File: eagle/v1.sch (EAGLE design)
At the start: 40 parts, among them IC2 LT1761, IC4 LT1376-ADJ, Q1 12Mhz, T1 Si2301DS, X1 USB-MICROB

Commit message: small change
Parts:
- R6: value 15k -> 680k
- R7: value 15k -> 220k
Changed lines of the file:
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@@
 <part name="SCK" library="wirepad" deviceset="SMD5" device=""/>
 <part name="L2" library="seb" deviceset="PIS2408" device="" value="20µH/xxx mA"/>
-<part name="R6" library="rcl" deviceset="R-EU_" device="R0402" value="15k"/>
-<part name="R7" library="rcl" deviceset="R-EU_" device="R0402" value="15k"/>
+<part name="R6" library="rcl" deviceset="R-EU_" device="R0402" value="680k"/>
+<part name="R7" library="rcl" deviceset="R-EU_" device="R0402" value="220k"/>
 <part name="GND6" library="supply1" deviceset="GND" device=""/>
 <part name="P+5" library="supply1" deviceset="+12V" device=""/>

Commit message: i2c connector
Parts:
- added 3V3, GN, SCL, SDA: (no value), wirepad:SMD2
- added C13: 1µF, SparkFun-Capacitors:CAP0805
- added R12, R13: 15k, rcl:R-EU_R0402
- added U$1: MAKE-DD_LOGO'PROMPT', seb:MAKE-DD_LOGO'PROMPT'
- renumbered BL/SW2 to BL
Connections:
- new net SCL: IC1.PIO0_4/SCL-(20MA_SINK), R13.2, SCL.P
- new net SDA: IC1.PIO0_5/SDA-(20MA_SINK), R12.2, SDA.P
- net +3V3: now also 3V3.P, R12.1, R13.1
- net ADC: now also C13.1
- net GND: now also C13.2, GN.P
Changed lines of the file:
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@@
 <part name="R5" library="rcl" deviceset="R-EU_" device="R0402" value="33R"/>
 <part name="RST" library="seb" deviceset="SWITCH_MCTAEF" device=""/>
-<part name="BL/SW2" library="seb" deviceset="SWITCH_MCTAEF" device=""/>
+<part name="BL" library="seb" deviceset="SWITCH_MCTAEF" device=""/>
 <part name="C3" library="rcl" deviceset="C-EU" device="C0402" value="22pF"/>
 <part name="C2" library="rcl" deviceset="C-EU" device="C0402" value="22pF"/>
@@
 <part name="GND7" library="supply1" deviceset="GND" device=""/>
 <part name="D1" library="seb" deviceset="DIODE_0805" device="" value="4148"/>
+<part name="C13" library="SparkFun-Capacitors" deviceset="CAP" device="0805" value="1µF"/>
+<part name="GND9" library="supply1" deviceset="GND" device=""/>
+<part name="U$1" library="seb" deviceset="MAKE-DD_LOGO" device="'PROMPT'"/>
+<part name="GN" library="wirepad" deviceset="SMD2" device=""/>
+<part name="3V3" library="wirepad" deviceset="SMD2" device=""/>
+<part name="SCL" library="wirepad" deviceset="SMD2" device=""/>
+<part name="SDA" library="wirepad" deviceset="SMD2" device=""/>
+<part name="GND13" library="supply1" deviceset="GND" device=""/>
+<part name="+3V6" library="supply1" deviceset="+3V3" device=""/>
+<part name="R12" library="rcl" deviceset="R-EU_" device="R0402" value="15k"/>
+<part name="R13" library="rcl" deviceset="R-EU_" device="R0402" value="15k"/>
 </parts>
 <sheets>
@@
 <attribute name="NAME" x="259.715" y="21.59" size="1.778" layer="95"/>
 </instance>
-<instance part="BL/SW2" gate="G$1" x="274.32" y="25.4" smashed="yes"/>
+<instance part="BL" gate="G$1" x="274.32" y="25.4" smashed="yes"/>
 <instance part="C3" gate="G$1" x="27.94" y="83.82" rot="R90"/>
 <instance part="C2" gate="G$1" x="27.94" y="88.9" rot="R90"/>
@@
 <instance part="P+6" gate="1" x="83.82" y="132.08"/>
 <instance part="GND7" gate="1" x="43.18" y="162.56"/>
+<instance part="C13" gate="G$1" x="93.98" y="109.22"/>
+<instance part="GND9" gate="1" x="93.98" y="104.14"/>
+<instance part="U$1" gate="G$1" x="274.32" y="-35.56"/>
+<instance part="GN" gate="1" x="132.08" y="160.02" rot="R180"/>
+<instance part="3V3" gate="1" x="132.08" y="152.4" rot="R180"/>
+<instance part="SCL" gate="1" x="132.08" y="144.78" rot="R180"/>
+<instance part="SDA" gate="1" x="132.08" y="137.16" rot="R180"/>
+<instance part="GND13" gate="1" x="114.3" y="160.02" rot="R270"/>
+<instance part="+3V6" gate="G$1" x="86.36" y="152.4" rot="R90"/>
+<instance part="R12" gate="G$1" x="99.06" y="137.16"/>
+<instance part="R13" gate="G$1" x="99.06" y="144.78"/>
 </instances>
 <busses>
@@
 <wire x1="259.08" y1="25.4" x2="269.24" y2="25.4" width="0.1524" layer="91"/>
 <pinref part="GND8" gate="1" pin="GND"/>
-<pinref part="BL/SW2" gate="G$1" pin="1"/>
+<pinref part="BL" gate="G$1" pin="1"/>
 </segment>
 <segment>
@@
 <junction x="43.18" y="165.1"/>
 </segment>
+<segment>
+<pinref part="C13" gate="G$1" pin="2"/>
+<pinref part="GND9" gate="1" pin="GND"/>
+</segment>
+<segment>
+<pinref part="GN" gate="1" pin="P"/>
+<wire x1="129.54" y1="160.02" x2="116.84" y2="160.02" width="0.1524" layer="91"/>
+<pinref part="GND13" gate="1" pin="GND"/>
+</segment>
 </net>
 <net name="+3V3" class="0">
@@
 <junction x="104.14" y="182.88"/>
 </segment>
+<segment>
+<pinref part="3V3" gate="1" pin="P"/>
+<wire x1="129.54" y1="152.4" x2="93.98" y2="152.4" width="0.1524" layer="91"/>
+<pinref part="+3V6" gate="G$1" pin="+3V3"/>
+<wire x1="93.98" y1="152.4" x2="88.9" y2="152.4" width="0.1524" layer="91"/>
+<wire x1="96.52" y1="144.78" x2="93.98" y2="144.78" width="0.1524" layer="91"/>
+<wire x1="93.98" y1="144.78" x2="93.98" y2="152.4" width="0.1524" layer="91"/>
+<junction x="93.98" y="152.4"/>
+<wire x1="96.52" y1="137.16" x2="93.98" y2="137.16" width="0.1524" layer="91"/>
+<wire x1="93.98" y1="137.16" x2="93.98" y2="144.78" width="0.1524" layer="91"/>
+<junction x="93.98" y="144.78"/>
+<pinref part="R12" gate="G$1" pin="1"/>
+<junction x="93.98" y="137.16"/>
+<pinref part="R13" gate="G$1" pin="1"/>
+</segment>
 </net>
 <net name="RST" class="0">
@@
 <segment>
 <wire x1="292.1" y1="25.4" x2="279.4" y2="25.4" width="0.1524" layer="91"/>
-<pinref part="BL/SW2" gate="G$1" pin="2"/>
+<pinref part="BL" gate="G$1" pin="2"/>
 <label x="287.02" y="25.4" size="1.778" layer="95"/>
 </segment>
@@
 <pinref part="R6" gate="G$1" pin="2"/>
 <pinref part="R7" gate="G$1" pin="2"/>
-<wire x1="83.82" y1="116.84" x2="91.44" y2="116.84" width="0.1524" layer="91"/>
+<wire x1="83.82" y1="116.84" x2="93.98" y2="116.84" width="0.1524" layer="91"/>
 <junction x="83.82" y="116.84"/>
 <label x="88.9" y="116.84" size="1.778" layer="95"/>
+<pinref part="C13" gate="G$1" pin="1"/>
+<wire x1="93.98" y1="114.3" x2="93.98" y2="116.84" width="0.1524" layer="91"/>
 </segment>
 <segment>
@@
 </segment>
 </net>
+<net name="SDA" class="0">
+<segment>
+<pinref part="SDA" gate="1" pin="P"/>
+<label x="116.84" y="137.16" size="1.778" layer="95"/>
+<wire x1="104.14" y1="137.16" x2="129.54" y2="137.16" width="0.1524" layer="91"/>
+<pinref part="R12" gate="G$1" pin="2"/>
+</segment>
+<segment>
+<pinref part="IC1" gate="G$1" pin="PIO0_5/SDA-(20MA_SINK)"/>
+<wire x1="119.38" y1="99.06" x2="109.22" y2="99.06" width="0.1524" layer="91"/>
+<label x="109.22" y="99.06" size="1.778" layer="95"/>
+</segment>
+</net>
+<net name="SCL" class="0">
+<segment>
+<pinref part="SCL" gate="1" pin="P"/>
+<label x="116.84" y="144.78" size="1.778" layer="95"/>
+<wire x1="129.54" y1="144.78" x2="104.14" y2="144.78" width="0.1524" layer="91"/>
+<pinref part="R13" gate="G$1" pin="2"/>
+</segment>
+<segment>
+<pinref part="IC1" gate="G$1" pin="PIO0_4/SCL-(20MA_SINK)"/>
+<wire x1="119.38" y1="101.6" x2="109.22" y2="101.6" width="0.1524" layer="91"/>
+<label x="109.22" y="101.6" size="1.778" layer="95"/>
+</segment>
+</net>

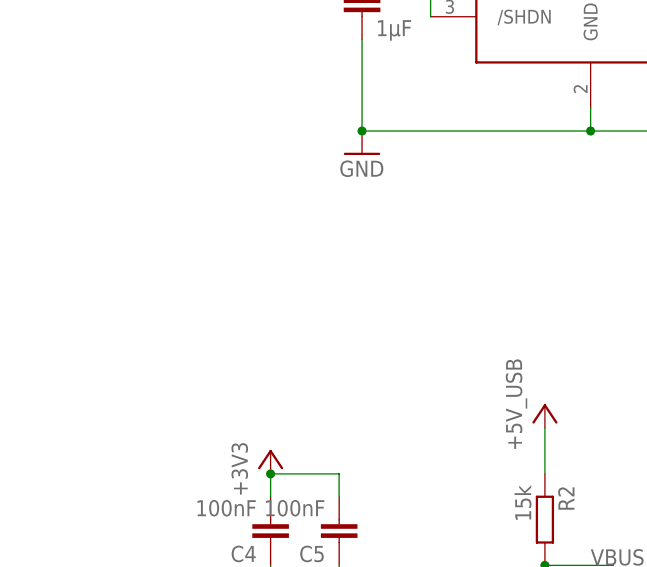
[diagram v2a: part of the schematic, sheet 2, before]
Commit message: supply circuit via USB for firmware upgrades
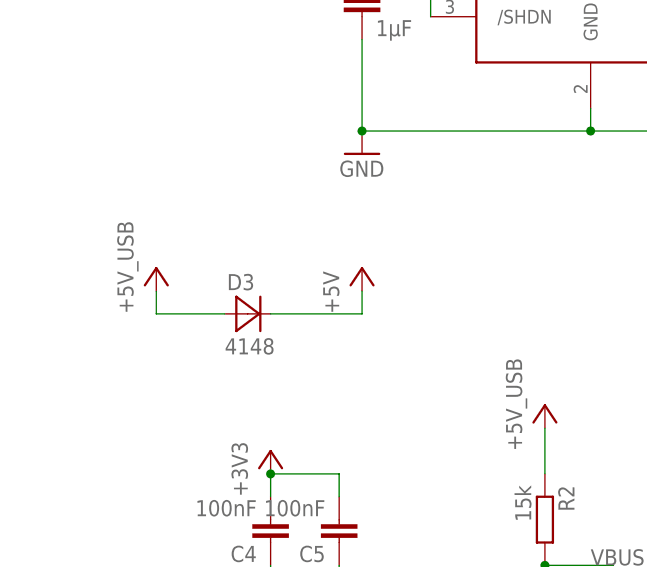
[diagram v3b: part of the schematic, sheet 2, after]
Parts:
- added D3: 4148, seb:DIODE_0805
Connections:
- net +5V: now also D3.C
- net +5V_USB: now also D3.A
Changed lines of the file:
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@@
 <?xml version="1.0" encoding="utf-8"?>
 <!DOCTYPE eagle SYSTEM "eagle.dtd">
-<eagle version="6.4">
+<eagle version="6.6.0">
 <drawing>
 <settings>
@@
 <part name="R12" library="rcl" deviceset="R-EU_" device="R0402" value="15k"/>
 <part name="R13" library="rcl" deviceset="R-EU_" device="R0402" value="15k"/>
+<part name="D3" library="seb" deviceset="DIODE_0805" device="" value="4148"/>
+<part name="P+8" library="supply1" deviceset="+5V" device=""/>
+<part name="P+7" library="supply1" deviceset="+5V" device="" value="+5V_USB"/>
 </parts>
 <sheets>
@@
 <instance part="R12" gate="G$1" x="99.06" y="137.16"/>
 <instance part="R13" gate="G$1" x="99.06" y="144.78"/>
+<instance part="D3" gate="G$1" x="30.48" y="144.78"/>
+<instance part="P+8" gate="1" x="43.18" y="149.86"/>
+<instance part="P+7" gate="1" x="20.32" y="149.86"/>
 </instances>
 <busses>
@@
 <wire x1="12.7" y1="48.26" x2="27.94" y2="48.26" width="0.1524" layer="91"/>
 </segment>
+<segment>
+<pinref part="P+7" gate="1" pin="+5V"/>
+<wire x1="20.32" y1="147.32" x2="20.32" y2="144.78" width="0.1524" layer="91"/>
+<pinref part="D3" gate="G$1" pin="A"/>
+<wire x1="20.32" y1="144.78" x2="27.94" y2="144.78" width="0.1524" layer="91"/>
+</segment>
 </net>
 <net name="01" class="0">
@@
 <junction x="43.18" y="182.88"/>
 </segment>
-</net>
+<segment>
+<pinref part="D3" gate="G$1" pin="C"/>
+<wire x1="33.02" y1="144.78" x2="43.18" y2="144.78" width="0.1524" layer="91"/>
+<pinref part="P+8" gate="1" pin="+5V"/>
+<wire x1="43.18" y1="144.78" x2="43.18" y2="147.32" width="0.1524" layer="91"/>
+</segment>
+</net>
